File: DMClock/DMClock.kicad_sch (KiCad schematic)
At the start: 10 parts, among them J5 Conn_01x07_Pin, J6 Conn_01x07_Pin

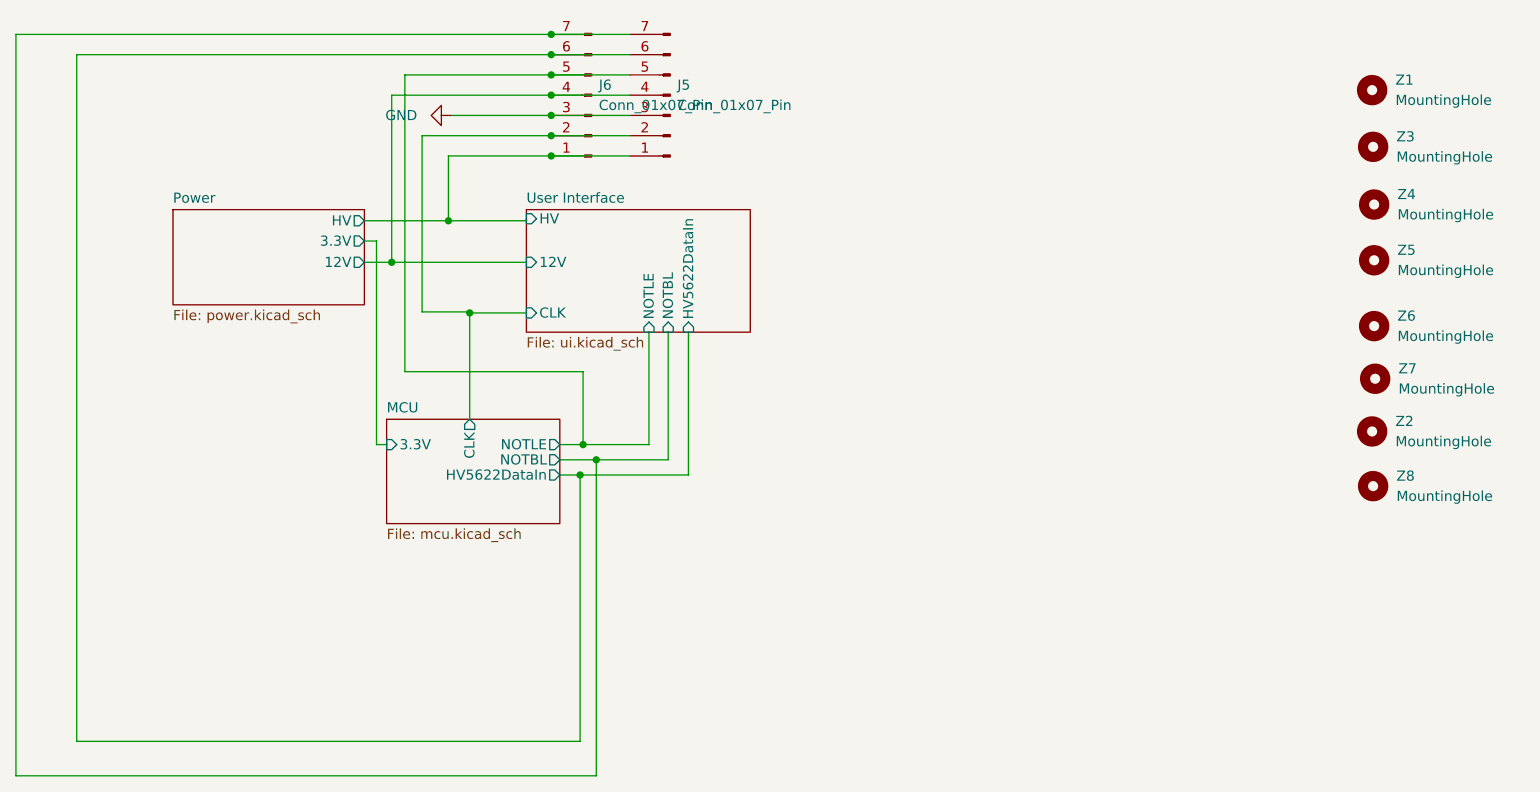
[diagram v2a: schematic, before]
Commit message: updated buck converter
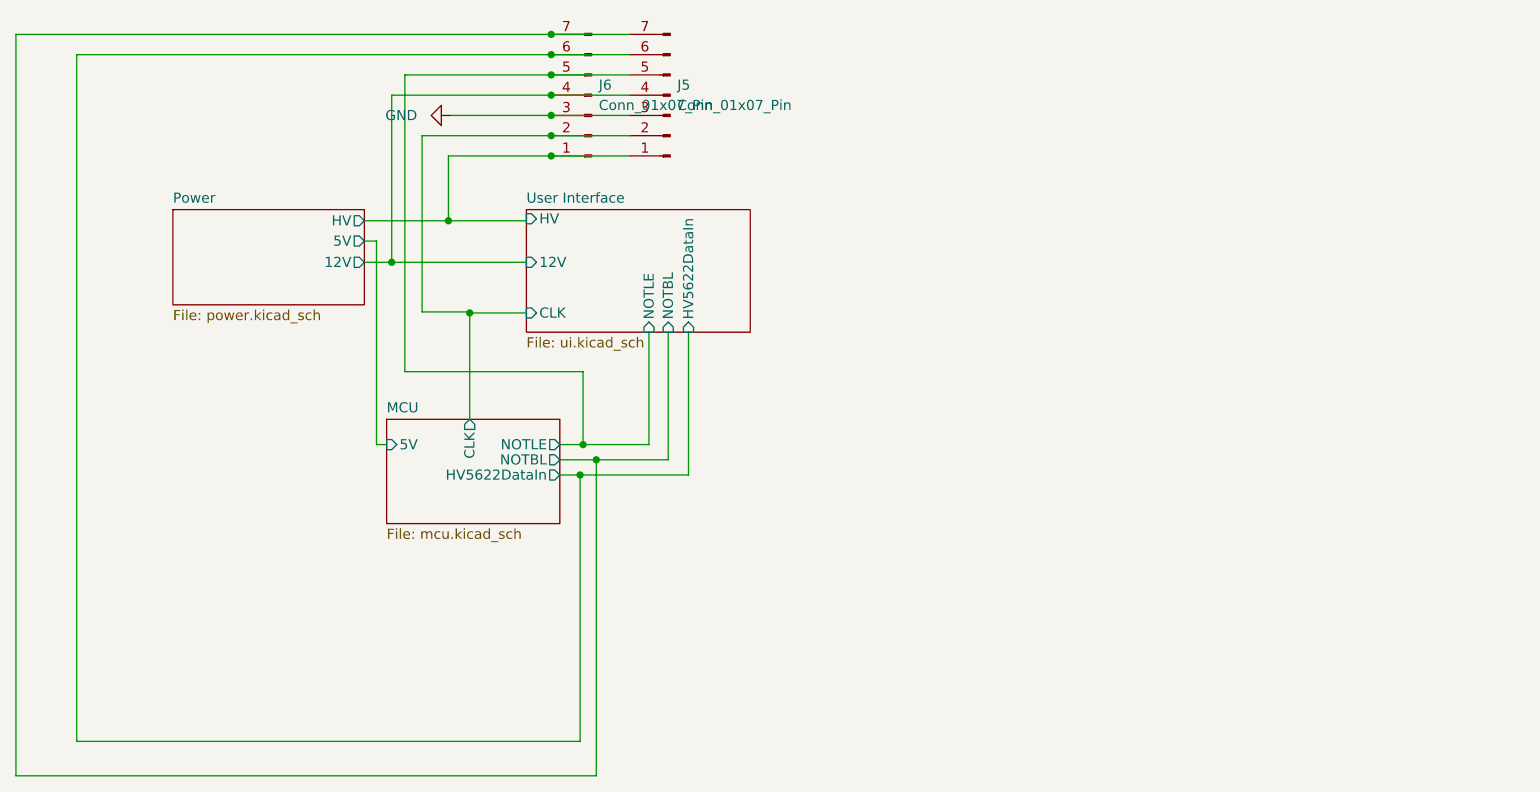
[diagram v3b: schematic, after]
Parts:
- removed Z1, Z2, Z3, Z4, Z5, Z6, Z7, Z8: MountingHole, MountingHole:MountingHole_2.2mm_M2, symbol Mechanical:MountingHole
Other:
- sheet MCU ports: added 5V; removed 3.3V
- sheet Power ports: added 5V; removed 3.3V
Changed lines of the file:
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@@
     (stroke (width 0) (type default))
-  )
-  (symbol (lib_id "Mechanical:MountingHole") (at 222.758 40.259 0) (unit 1)
-    (in_bom yes) (on_board yes) (dnp no)
-    (property "Reference" "Z3" (at 225.679 38.989 0)
-      (effects (font (size 1.27 1.27)) (justify left))
-    )
-    (property "Value" "MountingHole" (at 225.679 41.529 0)
-      (effects (font (size 1.27 1.27)) (justify left))
-    )
-    (property "Footprint" "MountingHole:MountingHole_2.2mm_M2" (at 222.758 40.259 0)
-      (effects (font (size 1.27 1.27)) hide)
-    )
-    (property "Datasheet" "~" (at 222.758 40.259 0)
-      (effects (font (size 1.27 1.27)) hide)
-    )
-    (instances
-      (project "DMClock"
-        (path "/b42b345f-a3f2-4eff-9109-2f4619119d33"
-          (reference "Z3") (unit 1)
-        )
-      )
-    )
-  )
-  (symbol (lib_id "Mechanical:MountingHole") (at 222.885 47.498 0) (unit 1)
-    (in_bom yes) (on_board yes) (dnp no)
-    (property "Reference" "Z4" (at 225.806 46.228 0)
-      (effects (font (size 1.27 1.27)) (justify left))
-    )
-    (property "Value" "MountingHole" (at 225.806 48.768 0)
-      (effects (font (size 1.27 1.27)) (justify left))
-    )
-    (property "Footprint" "MountingHole:MountingHole_2.2mm_M2" (at 222.885 47.498 0)
-      (effects (font (size 1.27 1.27)) hide)
-    )
-    (property "Datasheet" "~" (at 222.885 47.498 0)
-      (effects (font (size 1.27 1.27)) hide)
-    )
-    (instances
-      (project "DMClock"
-        (path "/b42b345f-a3f2-4eff-9109-2f4619119d33"
-          (reference "Z4") (unit 1)
-        )
-      )
-    )
-  )
-  (symbol (lib_id "Mechanical:MountingHole") (at 222.885 54.483 0) (unit 1)
-    (in_bom yes) (on_board yes) (dnp no)
-    (property "Reference" "Z5" (at 225.806 53.213 0)
-      (effects (font (size 1.27 1.27)) (justify left))
-    )
-    (property "Value" "MountingHole" (at 225.806 55.753 0)
-      (effects (font (size 1.27 1.27)) (justify left))
-    )
-    (property "Footprint" "MountingHole:MountingHole_2.2mm_M2" (at 222.885 54.483 0)
-      (effects (font (size 1.27 1.27)) hide)
-    )
-    (property "Datasheet" "~" (at 222.885 54.483 0)
-      (effects (font (size 1.27 1.27)) hide)
-    )
-    (instances
-      (project "DMClock"
-        (path "/b42b345f-a3f2-4eff-9109-2f4619119d33"
-          (reference "Z5") (unit 1)
-        )
-      )
-    )
   )
   (symbol (lib_id "Connector:Conn_01x07_Pin") (at 134.62 33.782 180) (unit 1)
@@
     )
   )
-  (symbol (lib_id "Mechanical:MountingHole") (at 223.012 69.342 0) (unit 1)
-    (in_bom yes) (on_board yes) (dnp no)
-    (property "Reference" "Z7" (at 225.933 68.072 0)
-      (effects (font (size 1.27 1.27)) (justify left))
-    )
-    (property "Value" "MountingHole" (at 225.933 70.612 0)
-      (effects (font (size 1.27 1.27)) (justify left))
-    )
-    (property "Footprint" "MountingHole:MountingHole_2.2mm_M2" (at 223.012 69.342 0)
-      (effects (font (size 1.27 1.27)) hide)
-    )
-    (property "Datasheet" "~" (at 223.012 69.342 0)
-      (effects (font (size 1.27 1.27)) hide)
-    )
-    (instances
-      (project "DMClock"
-        (path "/b42b345f-a3f2-4eff-9109-2f4619119d33"
-          (reference "Z7") (unit 1)
-        )
-      )
-    )
-  )
   (symbol (lib_id "power:GND") (at 107.188 36.322 270) (unit 1)
     (in_bom yes) (on_board yes) (dnp no) (fields_autoplaced)
@@
         (path "/b42b345f-a3f2-4eff-9109-2f4619119d33"
           (reference "#PWR06") (unit 1)
-        )
-      )
-    )
-  )
-  (symbol (lib_id "Mechanical:MountingHole") (at 222.631 33.147 0) (unit 1)
-    (in_bom yes) (on_board yes) (dnp no)
-    (property "Reference" "Z1" (at 225.552 31.877 0)
-      (effects (font (size 1.27 1.27)) (justify left))
-    )
-    (property "Value" "MountingHole" (at 225.552 34.417 0)
-      (effects (font (size 1.27 1.27)) (justify left))
-    )
-    (property "Footprint" "MountingHole:MountingHole_2.2mm_M2" (at 222.631 33.147 0)
-      (effects (font (size 1.27 1.27)) hide)
-    )
-    (property "Datasheet" "~" (at 222.631 33.147 0)
-      (effects (font (size 1.27 1.27)) hide)
-    )
-    (instances
-      (project "DMClock"
-        (path "/b42b345f-a3f2-4eff-9109-2f4619119d33"
-          (reference "Z1") (unit 1)
-        )
-      )
-    )
-  )
-  (symbol (lib_id "Mechanical:MountingHole") (at 222.631 75.946 0) (unit 1)
-    (in_bom yes) (on_board yes) (dnp no)
-    (property "Reference" "Z2" (at 225.552 74.676 0)
-      (effects (font (size 1.27 1.27)) (justify left))
-    )
-    (property "Value" "MountingHole" (at 225.552 77.216 0)
-      (effects (font (size 1.27 1.27)) (justify left))
-    )
-    (property "Footprint" "MountingHole:MountingHole_2.2mm_M2" (at 222.631 75.946 0)
-      (effects (font (size 1.27 1.27)) hide)
-    )
-    (property "Datasheet" "~" (at 222.631 75.946 0)
-      (effects (font (size 1.27 1.27)) hide)
-    )
-    (instances
-      (project "DMClock"
-        (path "/b42b345f-a3f2-4eff-9109-2f4619119d33"
-          (reference "Z2") (unit 1)
-        )
-      )
-    )
-  )
-  (symbol (lib_id "Mechanical:MountingHole") (at 222.885 62.738 0) (unit 1)
-    (in_bom yes) (on_board yes) (dnp no)
-    (property "Reference" "Z6" (at 225.806 61.468 0)
-      (effects (font (size 1.27 1.27)) (justify left))
-    )
-    (property "Value" "MountingHole" (at 225.806 64.008 0)
-      (effects (font (size 1.27 1.27)) (justify left))
-    )
-    (property "Footprint" "MountingHole:MountingHole_2.2mm_M2" (at 222.885 62.738 0)
-      (effects (font (size 1.27 1.27)) hide)
-    )
-    (property "Datasheet" "~" (at 222.885 62.738 0)
-      (effects (font (size 1.27 1.27)) hide)
-    )
-    (instances
-      (project "DMClock"
-        (path "/b42b345f-a3f2-4eff-9109-2f4619119d33"
-          (reference "Z6") (unit 1)
-        )
-      )
-    )
-  )
-  (symbol (lib_id "Mechanical:MountingHole") (at 222.758 82.804 0) (unit 1)
-    (in_bom yes) (on_board yes) (dnp no)
-    (property "Reference" "Z8" (at 225.679 81.534 0)
-      (effects (font (size 1.27 1.27)) (justify left))
-    )
-    (property "Value" "MountingHole" (at 225.679 84.074 0)
-      (effects (font (size 1.27 1.27)) (justify left))
-    )
-    (property "Footprint" "MountingHole:MountingHole_2.2mm_M2" (at 222.758 82.804 0)
-      (effects (font (size 1.27 1.27)) hide)
-    )
-    (property "Datasheet" "~" (at 222.758 82.804 0)
-      (effects (font (size 1.27 1.27)) hide)
-    )
-    (instances
-      (project "DMClock"
-        (path "/b42b345f-a3f2-4eff-9109-2f4619119d33"
-          (reference "Z8") (unit 1)
         )
       )
@@
       (effects (font (size 1.27 1.27)) (justify left top))
     )
-    (pin "3.3V" input (at 99.06 77.597 180)
+    (pin "5V" input (at 99.06 77.597 180)
       (effects (font (size 1.27 1.27)) (justify left))
     )
@@
       (effects (font (size 1.27 1.27)) (justify right))
     )
-    (pin "3.3V" output (at 96.266 52.07 0)
+    (pin "5V" output (at 96.266 52.07 0)
       (effects (font (size 1.27 1.27)) (justify right))
     )
